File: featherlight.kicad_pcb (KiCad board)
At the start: 4 copper layers, 50.8 x 50.8 mm, 105 parts, among them P1 USB_OTG, P11 CONN_01X06, P12 CONN_01X06, P13 CONN_01X06, P14 CONN_01X06, P15 CONN_01X06, P16 CONN_01X06, P17 CONN_01X06, P2 CONN_01X02, P3 CONN_01X01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

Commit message: Changed silkscreen of 220 uF cap to better highlight pin 1 polarity.
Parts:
- C31, C32: footprint Capacitors_Tantalum_SMD:TantalC_SizeD_EIA-7343_Reflow -> featherlight:TantalC_SizeD_EIA-7343_Reflow
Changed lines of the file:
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@@
     (pad 1 np_thru_hole circle (at 0 0) (size 2.2 2.2) (drill 2.2) (layers *.Cu *.Mask))
   )
-  (module Capacitors_Tantalum_SMD:TantalC_SizeD_EIA-7343_Reflow (layer B.Cu)
-    (at 92.71 105.664 180)
-    (descr "Tantal Cap. , Size D, EIA-7343, Reflow")
-    (tags "Tantal Capacitor Size-D EIA-7343 Reflow")
-    (attr smd)
-    (fp_text reference C31 (at -0.20066 3.29946 180) (layer B.SilkS) hide
-      (effects (font (size 1 1) (thickness 0.15)) (justify mirror))
-    )
-    (fp_text value "220 uF" (at -0.09906 -3.59918 180) (layer B.Fab)
-      (effects (font (size 1 1) (thickness 0.15)) (justify mirror))
-    )
-    (fp_line (start 4.6 2.6) (end -4.6 2.6) (layer B.CrtYd) (width 0.05))
-    (fp_line (start -4.6 2.6) (end -4.6 -2.6) (layer B.CrtYd) (width 0.05))
-    (fp_line (start -4.6 -2.6) (end 4.6 -2.6) (layer B.CrtYd) (width 0.05))
-    (fp_line (start 4.6 -2.6) (end 4.6 2.6) (layer B.CrtYd) (width 0.05))
-    (fp_line (start -4.2 -2.2) (end 3.8 -2.2) (layer B.SilkS) (width 0.15))
-    (fp_line (start 3.8 2.2) (end -4.3 2.2) (layer B.SilkS) (width 0.15))
-    (pad 1 smd rect (at -3.12 0 180) (size 2.37 2.43) (layers B.Cu B.Paste B.Mask)
-      (net 11 VDD))
-    (pad 2 smd rect (at 3.12 0 180) (size 2.37 2.43) (layers B.Cu B.Paste B.Mask)
-      (net 1 GND))
-    (model Capacitors_Tantalum_SMD.3dshapes/TantalC_SizeD_EIA-7343_Reflow.wrl
-      (at (xyz 0 0 0))
-      (scale (xyz 1 1 1))
-      (rotate (xyz 0 0 180))
-    )
-  )
   (module Adafruit:LED_SK6812MINI-PLCC4 (layer F.Cu)
     (at 80.979363 93.04626 337.5)
@@
     )
   )
-  (module Capacitors_Tantalum_SMD:TantalC_SizeD_EIA-7343_Reflow (layer B.Cu)
-    (at 93.472 94.234 90)
-    (descr "Tantal Cap. , Size D, EIA-7343, Reflow")
-    (tags "Tantal Capacitor Size-D EIA-7343 Reflow")
-    (attr smd)
-    (fp_text reference C32 (at -0.20066 3.29946 90) (layer B.SilkS) hide
-      (effects (font (size 1 1) (thickness 0.15)) (justify mirror))
-    )
-    (fp_text value "220 uF" (at -0.09906 -3.59918 90) (layer B.Fab)
-      (effects (font (size 1 1) (thickness 0.15)) (justify mirror))
-    )
-    (fp_line (start 4.6 2.6) (end -4.6 2.6) (layer B.CrtYd) (width 0.05))
-    (fp_line (start -4.6 2.6) (end -4.6 -2.6) (layer B.CrtYd) (width 0.05))
-    (fp_line (start -4.6 -2.6) (end 4.6 -2.6) (layer B.CrtYd) (width 0.05))
-    (fp_line (start 4.6 -2.6) (end 4.6 2.6) (layer B.CrtYd) (width 0.05))
-    (fp_line (start -4.2 -2.2) (end 3.8 -2.2) (layer B.SilkS) (width 0.15))
-    (fp_line (start 3.8 2.2) (end -4.3 2.2) (layer B.SilkS) (width 0.15))
-    (pad 1 smd rect (at -3.12 0 90) (size 2.37 2.43) (layers B.Cu B.Paste B.Mask)
-      (net 2 +3V3))
-    (pad 2 smd rect (at 3.12 0 90) (size 2.37 2.43) (layers B.Cu B.Paste B.Mask)
-      (net 1 GND))
-    (model Capacitors_Tantalum_SMD.3dshapes/TantalC_SizeD_EIA-7343_Reflow.wrl
-      (at (xyz 0 0 0))
-      (scale (xyz 1 1 1))
-      (rotate (xyz 0 0 180))
-    )
-  )
   (module featherlight:1812_PTC (layer F.Cu)
     (at 87.376 109.474 270)
@@
     )
   )
+  (module featherlight:TantalC_SizeD_EIA-7343_Reflow (layer B.Cu)
+    (at 92.71 105.664 180)
+    (descr "Tantal Cap. , Size D, EIA-7343, Reflow")
+    (tags "Tantal Capacitor Size-D EIA-7343 Reflow")
+    (attr smd)
+    (fp_text reference C31 (at -0.20066 -1.143 180) (layer B.SilkS) hide
+      (effects (font (size 1 1) (thickness 0.15)) (justify mirror))
+    )
+    (fp_text value "220 uF" (at -0.09906 -3.59918 180) (layer B.Fab)
+      (effects (font (size 1 1) (thickness 0.15)) (justify mirror))
+    )
+    (fp_line (start 4.6 2.6) (end -4.6 2.6) (layer B.CrtYd) (width 0.05))
+    (fp_line (start -4.6 2.6) (end -4.6 -2.6) (layer B.CrtYd) (width 0.05))
+    (fp_line (start -4.6 -2.6) (end 4.6 -2.6) (layer B.CrtYd) (width 0.05))
+    (fp_line (start 4.6 -2.6) (end 4.6 2.6) (layer B.CrtYd) (width 0.05))
+    (fp_line (start -4.2 -2.2) (end 3 -2.2) (layer B.SilkS) (width 0.15))
+    (fp_line (start 3 2.2) (end -4.3 2.2) (layer B.SilkS) (width 0.15))
+    (pad 2 smd rect (at 3.12 0 180) (size 2.37 2.43) (layers B.Cu B.Paste B.Mask)
+      (net 1 GND))
+    (pad 1 smd rect (at -3.12 0 180) (size 2.37 2.43) (layers B.Cu B.Paste B.Mask)
+      (net 11 VDD))
+    (model Capacitors_Tantalum_SMD.3dshapes/TantalC_SizeD_EIA-7343_Reflow.wrl
+      (at (xyz 0 0 0))
+      (scale (xyz 1 1 1))
+      (rotate (xyz 0 0 180))
+    )
+  )
+  (module featherlight:TantalC_SizeD_EIA-7343_Reflow (layer B.Cu)
+    (at 93.472 94.234 90)
+    (descr "Tantal Cap. , Size D, EIA-7343, Reflow")
+    (tags "Tantal Capacitor Size-D EIA-7343 Reflow")
+    (attr smd)
+    (fp_text reference C32 (at -0.20066 -1.143 90) (layer B.SilkS) hide
+      (effects (font (size 1 1) (thickness 0.15)) (justify mirror))
+    )
+    (fp_text value "220 uF" (at -0.09906 -3.59918 90) (layer B.Fab)
+      (effects (font (size 1 1) (thickness 0.15)) (justify mirror))
+    )
+    (fp_line (start 3 2.2) (end -4.3 2.2) (layer B.SilkS) (width 0.15))
+    (fp_line (start -4.2 -2.2) (end 3 -2.2) (layer B.SilkS) (width 0.15))
+    (fp_line (start 4.6 -2.6) (end 4.6 2.6) (layer B.CrtYd) (width 0.05))
+    (fp_line (start -4.6 -2.6) (end 4.6 -2.6) (layer B.CrtYd) (width 0.05))
+    (fp_line (start -4.6 2.6) (end -4.6 -2.6) (layer B.CrtYd) (width 0.05))
+    (fp_line (start 4.6 2.6) (end -4.6 2.6) (layer B.CrtYd) (width 0.05))
+    (pad 1 smd rect (at -3.12 0 90) (size 2.37 2.43) (layers B.Cu B.Paste B.Mask)
+      (net 2 +3V3))
+    (pad 2 smd rect (at 3.12 0 90) (size 2.37 2.43) (layers B.Cu B.Paste B.Mask)
+      (net 1 GND))
+    (model Capacitors_Tantalum_SMD.3dshapes/TantalC_SizeD_EIA-7343_Reflow.wrl
+      (at (xyz 0 0 0))
+      (scale (xyz 1 1 1))
+      (rotate (xyz 0 0 180))
+    )
+  )

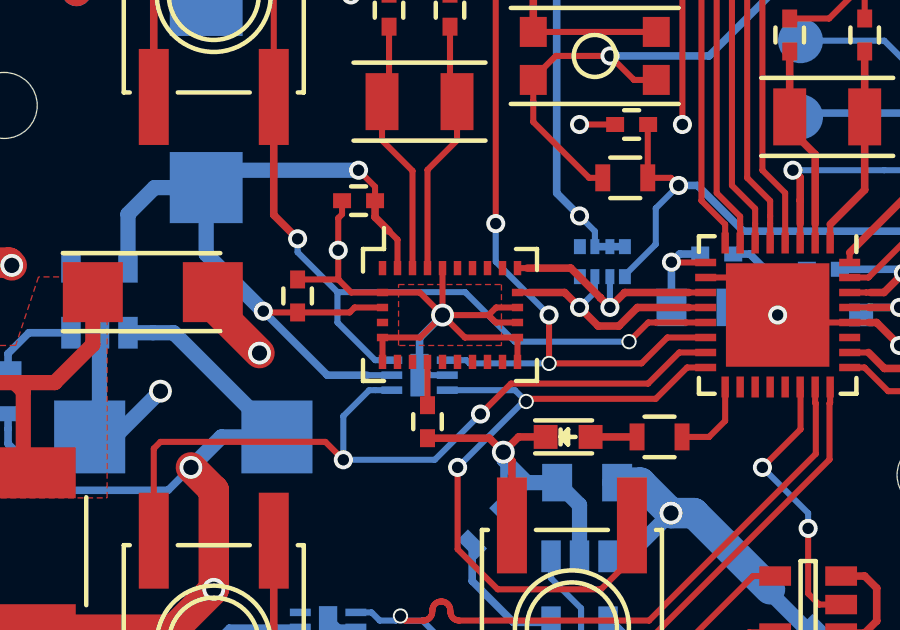
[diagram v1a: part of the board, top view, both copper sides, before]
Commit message: Changed pad and mask geometry of BNO055 footprint based on manufacturer guidelines (ref. Handling, soldering & mounting instructions for BNO055).
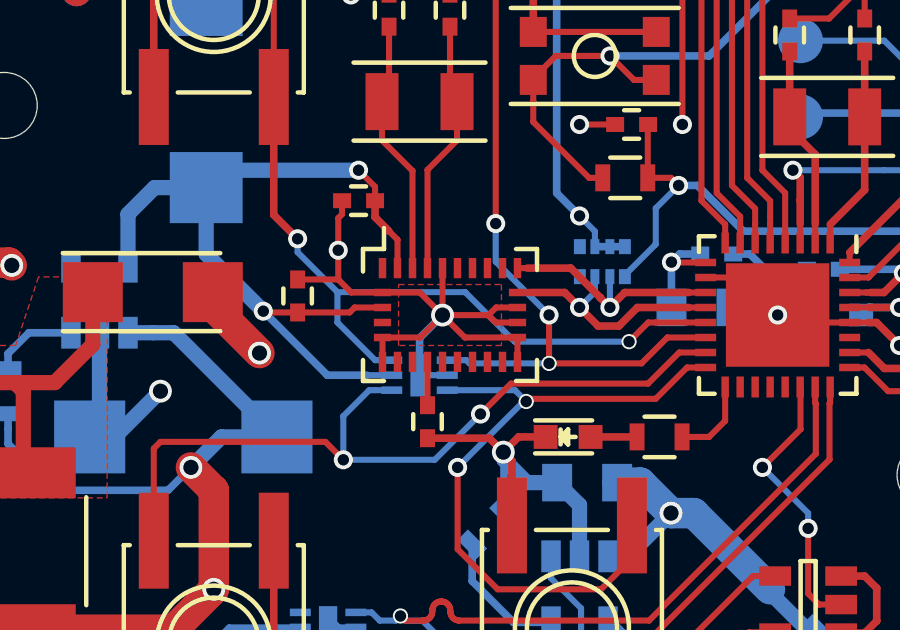
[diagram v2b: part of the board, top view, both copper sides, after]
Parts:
- U1: footprint Housings_LGA:LGA-28 -> featherlight:LGA-28
- turned U1 to 0 degrees
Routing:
- net /MCU + IMU/SCL: track 8.23 -> 14.8 mm, vias 1 -> 0
- net GND: track 302.5 -> 299.3 mm, vias 32 -> 33
- net /MCU + IMU/SDA: track 8.05 -> 4.87 mm
- net Net-(C12-Pad1): track 1.44 -> 0.00 mm
- net (no net): track 0.00 -> 1.44 mm

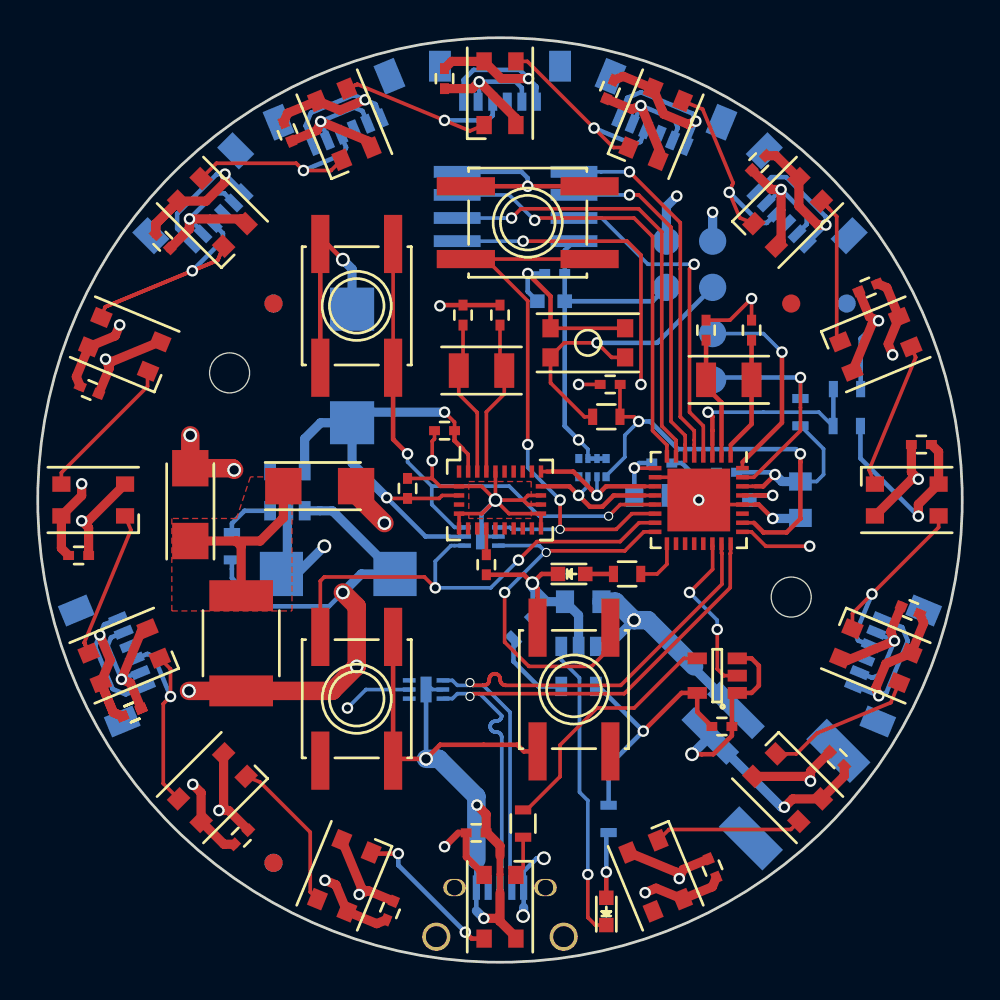
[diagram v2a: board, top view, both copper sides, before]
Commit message: Extensive revisions of PCB connecting and near the BNO055 after issues with rev C and finding relevant design notes.
    -Top copper layer below the sensor is now a keep out zone.  This required extensive trace rerouting due to all the pins tied to ground.
    -Added pullups to the bootloader and reset pins (they were previously floating).  Expect this was the main reason I could never get it to initialize.
    -Added pulldown to I2C address selection pin (it was previously directly connected).  It's what Adafruit does and I had an extra lane in the nearby resistor pack.
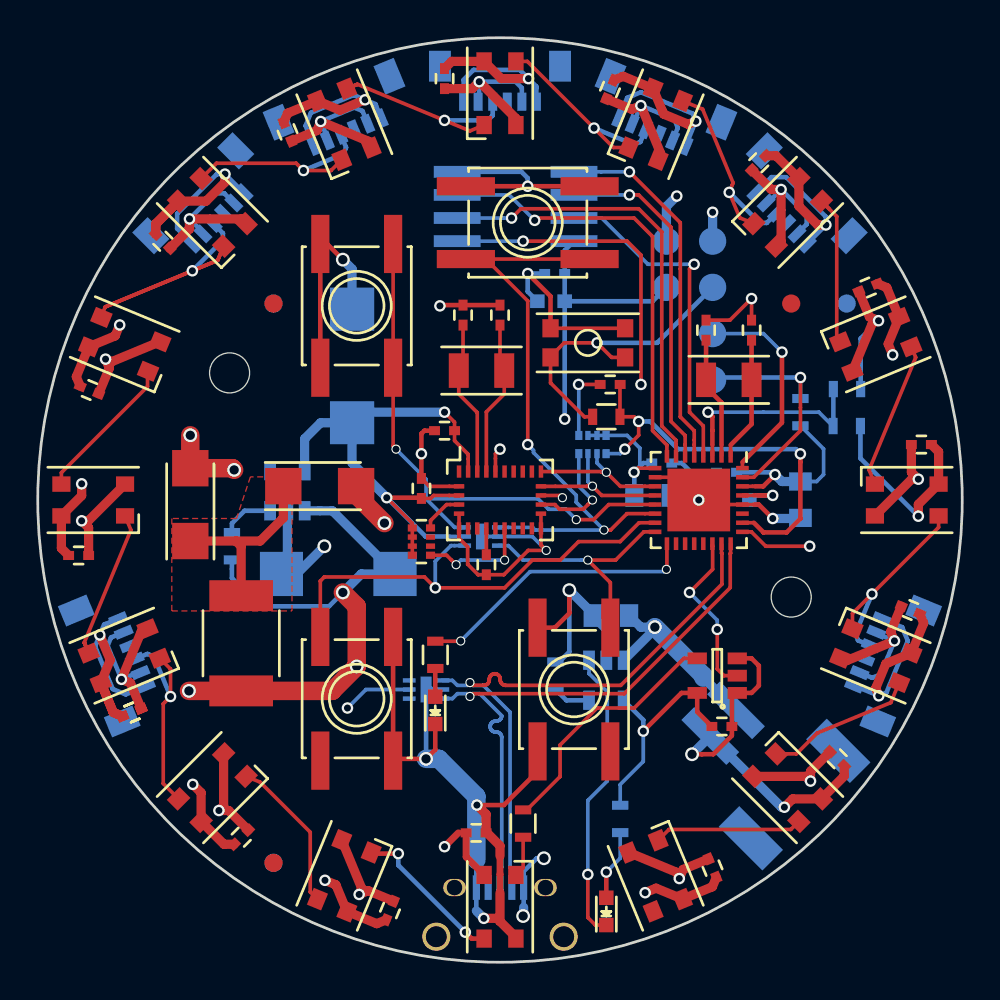
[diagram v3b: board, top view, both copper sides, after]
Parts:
- added RN2: 10 K, Resistors_SMD:R_Array_Convex_4x0402, F.Cu at (97.3, 103.9)
- moved R3 11.4 mm to (98.0, 110.1), turned to 90 degrees
- moved D22 10.6 mm to (98.0, 113.2), turned to 90 degrees
- moved R14 3.10 mm to (104.6, 111.3), turned to 90 degrees
- moved C33 1.70 mm to (107.7, 108.0)
- moved U5 1.70 mm to (107.4, 111.5)
- moved RN1 1.27 mm to (106.7, 98.6)
- moved C3 0.76 mm to (97.3, 101.0)
- moved R12 0.63 mm to (108.2, 119.1)
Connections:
- net Net-(C9-Pad1) renamed /MCU + IMU/ATMEL_RESET
- RN1 pad 4: (no net) -> /MCU + IMU/BNO_I2C_ADDR
- RN1 pad 5: (no net) -> GND
- U1 pad 11: (no net) -> /MCU + IMU/BNO_RESET
- U1 pad 17: GND -> /MCU + IMU/BNO_I2C_ADDR
- U1 pad 4: (no net) -> /MCU + IMU/BNO_BOOTLOAD
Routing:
- net Net-(R3-Pad2): track 2.79 -> 15.8 mm, vias 0 -> 2
- net LR_BUTTON: track 23.1 -> 13.8 mm, vias 2 -> 1
- net /MCU + IMU/SCL: track 14.8 -> 8.38 mm, vias 0 -> 1
- net /MCU + IMU/BNO_RESET: track 0.00 -> 6.13 mm, vias 0 -> 2
- net /MCU + IMU/BNO_I2C_ADDR: track 0.00 -> 6.01 mm, vias 0 -> 1
- net +3V3: track 61.5 -> 66.7 mm
- net GND: track 299.3 -> 304.2 mm, vias 33 -> 34
- net /MCU + IMU/SDA: track 4.87 -> 7.84 mm
- net /MCU + IMU/BNO_BOOTLOAD: track 0.00 -> 2.34 mm
- net Net-(R14-Pad1): track 4.42 -> 2.09 mm
- net VDD: track 174.9 -> 173.3 mm
- net Net-(C12-Pad1): track 0.00 -> 1.44 mm
- net (no net): track 1.44 -> 0.00 mm
- net UR_BUTTON: track 33.5 -> 34.5 mm, vias 3 -> 2
- net /MCU + IMU/ATMEL_RESET: track 23.6 -> 22.8 mm, vias 2 -> 3
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- removed copper zone on F.Cu, net GND

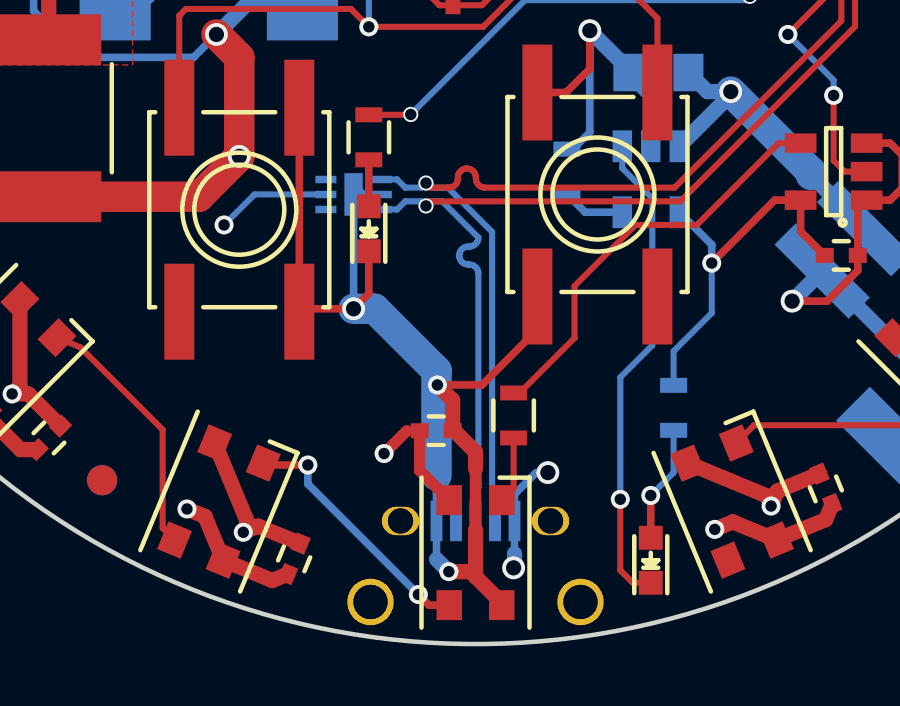
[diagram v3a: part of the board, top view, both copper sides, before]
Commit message: Moved USB port inwards slightly after noticing damage to the outer PTH on rev C boards.
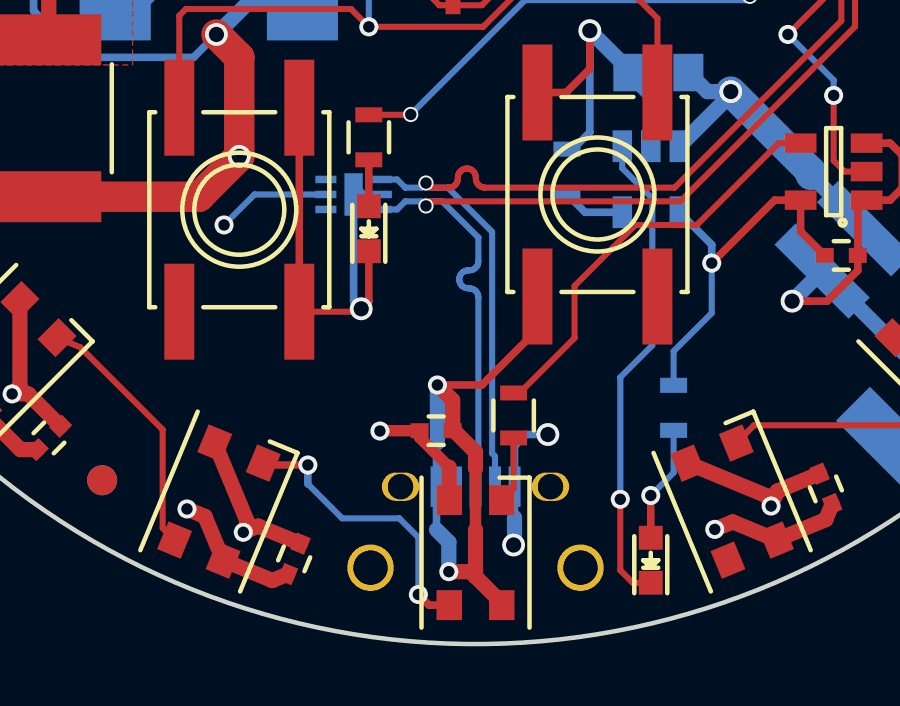
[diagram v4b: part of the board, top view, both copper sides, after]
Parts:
- moved P1 1.14 mm to (101.6, 123.3)
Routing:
- net GND: track 304.2 -> 300.6 mm
- net D-: track 33.4 -> 32.3 mm
- net D+: track 33.4 -> 32.3 mm
- net /LED Array/D1D0: track 8.53 -> 9.65 mm
- net /Power Regulation & Distribution/VUSB: track 50.0 -> 50.6 mm

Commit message: Grounded USB shield after issues with programming MCU over USB.
The Atmel design notes recommend grounding through an RC filter, but Adafruit ignores it, and that's good enough for me.
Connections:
- P1 pad 6: Net-(P1-Pad6) -> GND

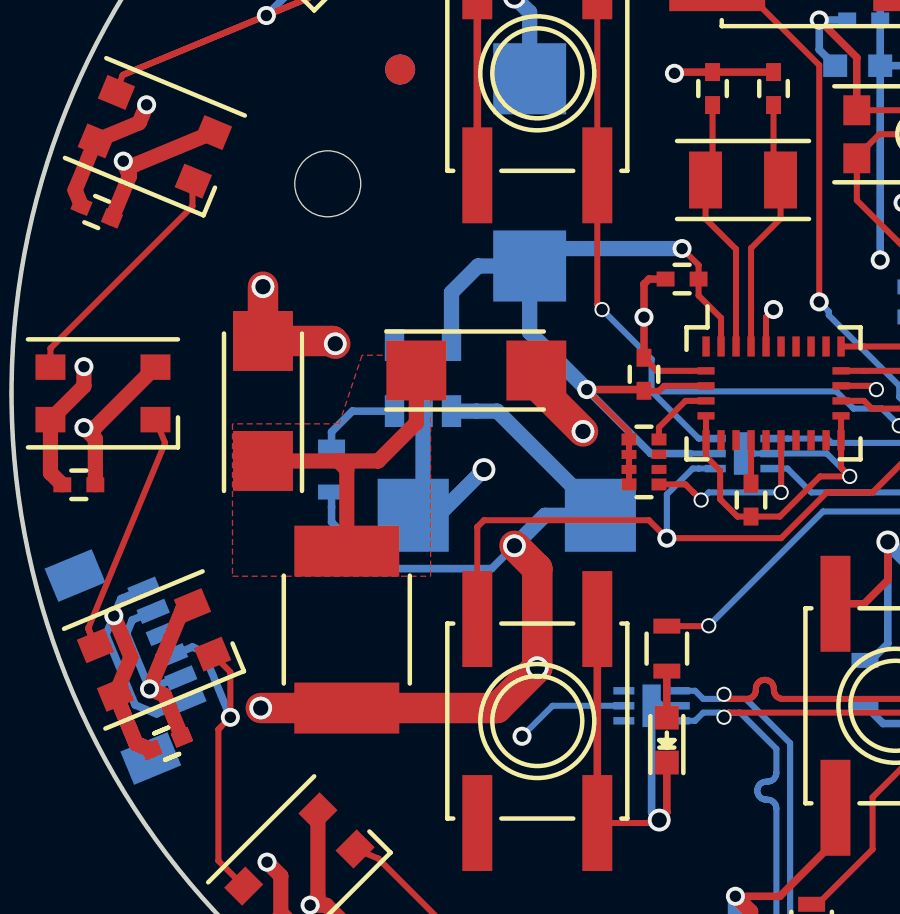
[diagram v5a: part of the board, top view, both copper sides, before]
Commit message: Rotated the power diodes and fuse since the spiralling traces bothered me.
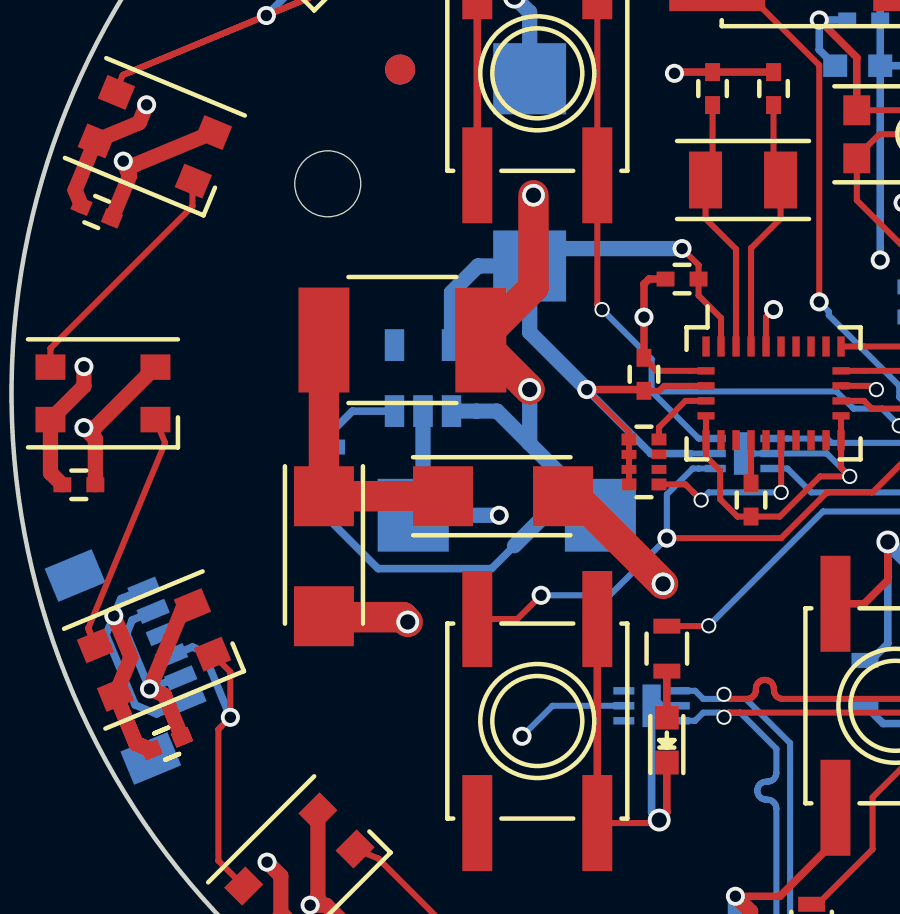
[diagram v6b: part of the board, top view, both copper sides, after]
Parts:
- moved F1 9.83 mm to (89.2, 99.8), turned to 0 degrees
- moved D24 5.56 mm to (86.6, 107.0), turned to 270 degrees
- moved D20 4.28 mm to (92.6, 105.0)
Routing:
- net /Power Regulation & Distribution/VUSB: track 50.6 -> 36.0 mm, vias 5 -> 4
- net VDD: track 173.2 -> 168.7 mm, vias 21 -> 20
- net +BATT: track 31.9 -> 27.6 mm
- net LL_BUTTON: track 26.8 -> 24.5 mm, vias 1 -> 2
- net /Power Regulation & Distribution/VFUSE: track 10.5 -> 9.18 mm
- removed copper zone on F.Cu, net /Power Regulation & Distribution/VFUSE
